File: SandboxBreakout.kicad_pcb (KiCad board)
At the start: 2 copper layers, 58 parts

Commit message: Board Draft 1.0
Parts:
- 12C_2, ADC3.3_2, ADC6.6_2, Can2, GPS2, Pow2, SPI2, SPKT2, Serial2, Switch2, Telem2, Telem4, USB2: moved to F.Cu
- moved 12C_2 110.7 mm to (80.1, 127.1)
- moved Pow1 110.6 mm to (119.4, 118.1)
- moved Pow2 110.6 mm to (119.4, 127.0)
- moved USB2 110.6 mm to (62.2, 127.0)
- moved 12C_1 110.6 mm to (80.0, 118.1)
- moved ADC3.3_1 110.6 mm to (27.9, 118.1)
- moved ADC3.3_2 110.6 mm to (27.9, 127.0)
- moved ADC6.6_1 110.6 mm to (138.4, 118.1)
- moved ADC6.6_2 110.6 mm to (138.4, 127.0)
- moved Can1 110.6 mm to (45.7, 118.1)
- moved Can2 110.6 mm to (45.7, 127.0)
- moved SPI1 110.6 mm to (99.1, 118.1)
- moved SPI2 110.6 mm to (99.1, 127.0)
- moved USB1 110.6 mm to (62.1, 118.2)
- moved Servo31 27.0 mm to (82.5, 74.9)
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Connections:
- Servo10 pad 2: Net-(Servo10-Pad2) -> Net-(Servo1-Pad2)
- Servo10 pad 3: Net-(Servo10-Pad3) -> Net-(Servo1-Pad3)
- Servo11 pad 2: Net-(Servo11-Pad2) -> Net-(Servo1-Pad2)
- Servo11 pad 3: Net-(Servo11-Pad3) -> Net-(Servo1-Pad3)
- Servo12 pad 2: Net-(Servo11-Pad2) -> Net-(Servo1-Pad2)
- Servo12 pad 3: Net-(Servo11-Pad3) -> Net-(Servo1-Pad3)
- Servo13 pad 2: Net-(Servo13-Pad2) -> Net-(Servo1-Pad2)
- Servo13 pad 3: Net-(Servo13-Pad3) -> Net-(Servo1-Pad3)
- Servo14 pad 2: Net-(Servo13-Pad2) -> Net-(Servo1-Pad2)
- Servo14 pad 3: Net-(Servo13-Pad3) -> Net-(Servo1-Pad3)
- Servo15 pad 2: Net-(Servo15-Pad2) -> Net-(Servo1-Pad2)
- Servo15 pad 3: Net-(Servo15-Pad3) -> Net-(Servo1-Pad3)
- Servo16 pad 2: Net-(Servo15-Pad2) -> Net-(Servo1-Pad2)
- Servo16 pad 3: Net-(Servo15-Pad3) -> Net-(Servo1-Pad3)
- Servo17 pad 2: Net-(Servo17-Pad2) -> Net-(Servo1-Pad2)
- Servo17 pad 3: Net-(Servo17-Pad3) -> Net-(Servo1-Pad3)
- Servo18 pad 2: Net-(Servo17-Pad2) -> Net-(Servo1-Pad2)
- Servo18 pad 3: Net-(Servo17-Pad3) -> Net-(Servo1-Pad3)
- Servo19 pad 2: Net-(Servo19-Pad2) -> Net-(Servo1-Pad2)
- Servo19 pad 3: Net-(Servo19-Pad3) -> Net-(Servo1-Pad3)
- Servo20 pad 2: Net-(Servo19-Pad2) -> Net-(Servo1-Pad2)
- Servo20 pad 3: Net-(Servo19-Pad3) -> Net-(Servo1-Pad3)
- Servo21 pad 2: Net-(Servo21-Pad2) -> Net-(Servo1-Pad2)
- Servo21 pad 3: Net-(Servo21-Pad3) -> Net-(Servo1-Pad3)
- Servo22 pad 2: Net-(Servo21-Pad2) -> Net-(Servo1-Pad2)
- Servo22 pad 3: Net-(Servo21-Pad3) -> Net-(Servo1-Pad3)
- Servo23 pad 2: Net-(Servo23-Pad2) -> Net-(Servo1-Pad2)
- Servo23 pad 3: Net-(Servo23-Pad3) -> Net-(Servo1-Pad3)
- Servo24 pad 2: Net-(Servo23-Pad2) -> Net-(Servo1-Pad2)
- Servo24 pad 3: Net-(Servo23-Pad3) -> Net-(Servo1-Pad3)
- Servo25 pad 2: Net-(Servo25-Pad2) -> Net-(Servo1-Pad2)
- Servo25 pad 3: Net-(Servo25-Pad3) -> Net-(Servo1-Pad3)
- Servo26 pad 2: Net-(Servo25-Pad2) -> Net-(Servo1-Pad2)
- Servo26 pad 3: Net-(Servo25-Pad3) -> Net-(Servo1-Pad3)
- Servo27 pad 2: Net-(Servo27-Pad2) -> Net-(Servo1-Pad2)
- Servo27 pad 3: Net-(Servo27-Pad3) -> Net-(Servo1-Pad3)
- Servo28 pad 2: Net-(Servo27-Pad2) -> Net-(Servo1-Pad2)
- Servo28 pad 3: Net-(Servo27-Pad3) -> Net-(Servo1-Pad3)
- Servo29 pad 2: Net-(Servo29-Pad2) -> Net-(Servo1-Pad2)
- Servo29 pad 3: Net-(Servo29-Pad3) -> Net-(Servo1-Pad3)
- Servo3 pad 2: Net-(Servo3-Pad2) -> Net-(Servo1-Pad2)
- Servo3 pad 3: Net-(Servo3-Pad3) -> Net-(Servo1-Pad3)
- Servo30 pad 2: Net-(Servo29-Pad2) -> Net-(Servo1-Pad2)
- Servo30 pad 3: Net-(Servo29-Pad3) -> Net-(Servo1-Pad3)
- Servo31 pad 2: Net-(Servo31-Pad2) -> Net-(Servo1-Pad2)
- Servo31 pad 3: Net-(Servo31-Pad3) -> Net-(Servo1-Pad3)
- Servo32 pad 2: Net-(Servo31-Pad2) -> Net-(Servo1-Pad2)
- Servo32 pad 3: Net-(Servo31-Pad3) -> Net-(Servo1-Pad3)
- Servo4 pad 2: Net-(Servo3-Pad2) -> Net-(Servo1-Pad2)
- Servo4 pad 3: Net-(Servo3-Pad3) -> Net-(Servo1-Pad3)
- Servo5 pad 2: Net-(Servo5-Pad2) -> Net-(Servo1-Pad2)
- Servo5 pad 3: Net-(Servo5-Pad3) -> Net-(Servo1-Pad3)
- Servo6 pad 2: Net-(Servo5-Pad2) -> Net-(Servo1-Pad2)
- Servo6 pad 3: Net-(Servo5-Pad3) -> Net-(Servo1-Pad3)
- Servo7 pad 2: Net-(Servo7-Pad2) -> Net-(Servo1-Pad2)
- Servo7 pad 3: Net-(Servo7-Pad3) -> Net-(Servo1-Pad3)
- Servo8 pad 2: Net-(Servo7-Pad2) -> Net-(Servo1-Pad2)
- Servo8 pad 3: Net-(Servo7-Pad3) -> Net-(Servo1-Pad3)
- Servo9 pad 2: Net-(Servo10-Pad2) -> Net-(Servo1-Pad2)
- Servo9 pad 3: Net-(Servo10-Pad3) -> Net-(Servo1-Pad3)
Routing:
- net Net-(Servo1-Pad3): track 0.00 -> 139.8 mm
- net Net-(Servo1-Pad2): track 0.00 -> 137.6 mm
- net Net-(Servo29-Pad1): track 0.00 -> 23.8 mm
- net Net-(Servo7-Pad1): track 0.00 -> 23.8 mm
- net Net-(Servo17-Pad1): track 0.00 -> 23.8 mm
- net Net-(Servo13-Pad1): track 0.00 -> 23.8 mm
- net Net-(Servo27-Pad1): track 0.00 -> 23.8 mm
- net Net-(Servo25-Pad1): track 0.00 -> 23.8 mm
- net Net-(Servo23-Pad1): track 0.00 -> 23.8 mm
- net Net-(Servo5-Pad1): track 0.00 -> 23.8 mm
- net Net-(Servo31-Pad1): track 0.00 -> 23.8 mm
- net Net-(Servo3-Pad1): track 0.00 -> 23.8 mm
- net Net-(Servo21-Pad1): track 0.00 -> 23.8 mm
- net Net-(Servo19-Pad1): track 0.00 -> 23.8 mm
- net Net-(Servo15-Pad1): track 0.00 -> 23.8 mm
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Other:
- board outline added: 129.5 x 88.9 mm

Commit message: flipped a footprint
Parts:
- Servo2: moved to F.Cu
- turned Servo2 to 0 degrees

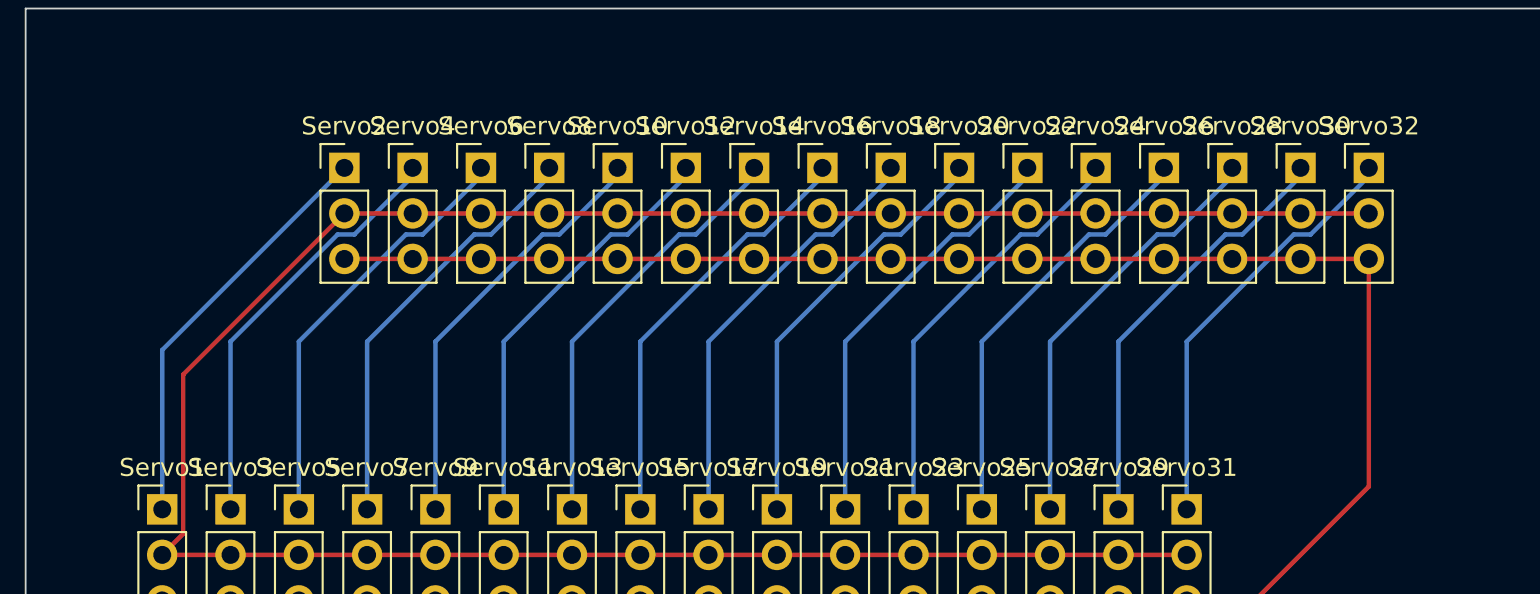
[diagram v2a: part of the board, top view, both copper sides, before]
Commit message: Updated labels
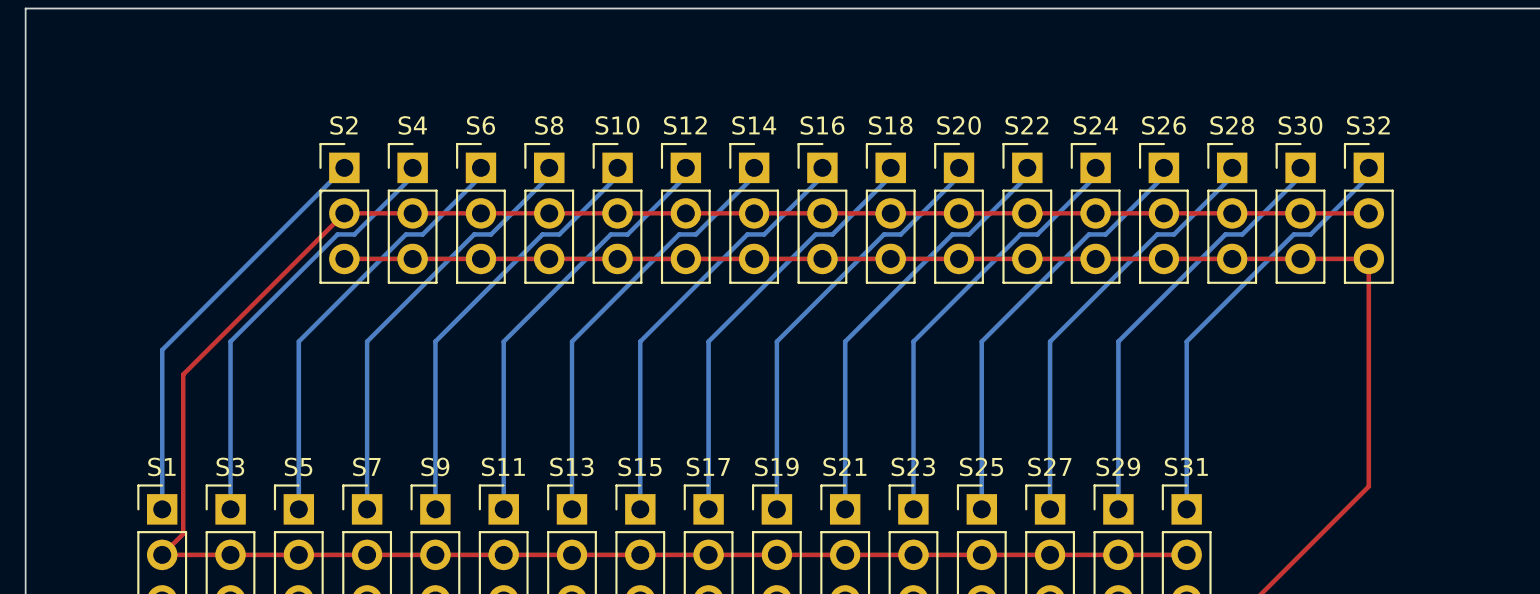
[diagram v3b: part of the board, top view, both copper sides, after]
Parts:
- renumbered Servo1 to S1, Servo10 to S10, Servo11 to S11, Servo12 to S12, Servo13 to S13, Servo14 to S14, Servo15 to S15, Servo16 to S16, Servo17 to S17, Servo18 to S18, Servo19 to S19, Servo2 to S2, Servo20 to S20, Servo21 to S21, Servo22 to S22, Servo23 to S23, Servo24 to S24, Servo25 to S25, Servo26 to S26, Servo27 to S27, Servo28 to S28, Servo29 to S29, Servo3 to S3, Servo30 to S30, Servo31 to S31, Servo32 to S32, Servo4 to S4, Servo5 to S5, Servo6 to S6, Servo7 to S7, Servo8 to S8, Servo9 to S9

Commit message: Added gerber and drill files
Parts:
- moved S31 19.0 mm to (63.5, 74.9)
- moved S32 19.0 mm to (73.7, 55.9)
- moved S30 17.8 mm to (71.1, 55.9)
- moved S29 17.8 mm to (61.0, 74.9)
- moved S27 16.5 mm to (58.4, 74.9)
- moved S28 16.5 mm to (68.6, 55.9)
- moved S25 15.2 mm to (55.9, 74.9)
- moved S26 15.2 mm to (66.0, 55.9)
- moved S23 14.0 mm to (53.3, 74.9)
- moved S24 14.0 mm to (63.5, 55.9)
- moved S21 12.7 mm to (50.8, 74.9)
- moved S22 12.7 mm to (61.0, 55.9)
- moved S19 11.4 mm to (48.3, 74.9)
- moved S20 11.4 mm to (58.4, 55.9)
- moved S17 10.2 mm to (45.7, 74.9)
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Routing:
- net Net-(S1-Pad3): track 139.8 -> 99.5 mm
- net Net-(S1-Pad2): track 137.6 -> 99.5 mm
- net Net-(S29-Pad1): track 23.8 -> 23.3 mm
- net Net-(S7-Pad1): track 23.8 -> 23.3 mm
- net Net-(S17-Pad1): track 23.8 -> 23.3 mm
- net Net-(S13-Pad1): track 23.8 -> 23.3 mm
- net Net-(S31-Pad1): track 23.8 -> 23.3 mm
- net Net-(S27-Pad1): track 23.8 -> 23.3 mm
- net Net-(S25-Pad1): track 23.8 -> 23.3 mm
- net Net-(S23-Pad1): track 23.8 -> 23.3 mm
- net Net-(S11-Pad1): track 23.8 -> 23.3 mm
- net Net-(S10-Pad1): track 23.8 -> 23.3 mm
- net Net-(S5-Pad1): track 23.8 -> 23.3 mm
- net Net-(S3-Pad1): track 23.8 -> 23.3 mm
- net Net-(S21-Pad1): track 23.8 -> 23.3 mm
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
